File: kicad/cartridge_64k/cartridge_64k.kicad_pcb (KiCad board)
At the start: 2 copper layers, 39 x 102.2 mm, 12 parts, among them J1 Card edge (87715-9106 mate), U1 ATF22V10C-7PX, U2 AT28C256-15PU, U3 AT28C256-15PU, U4 AS7C256C-15PCN, U5 AS7C256C-15PCN

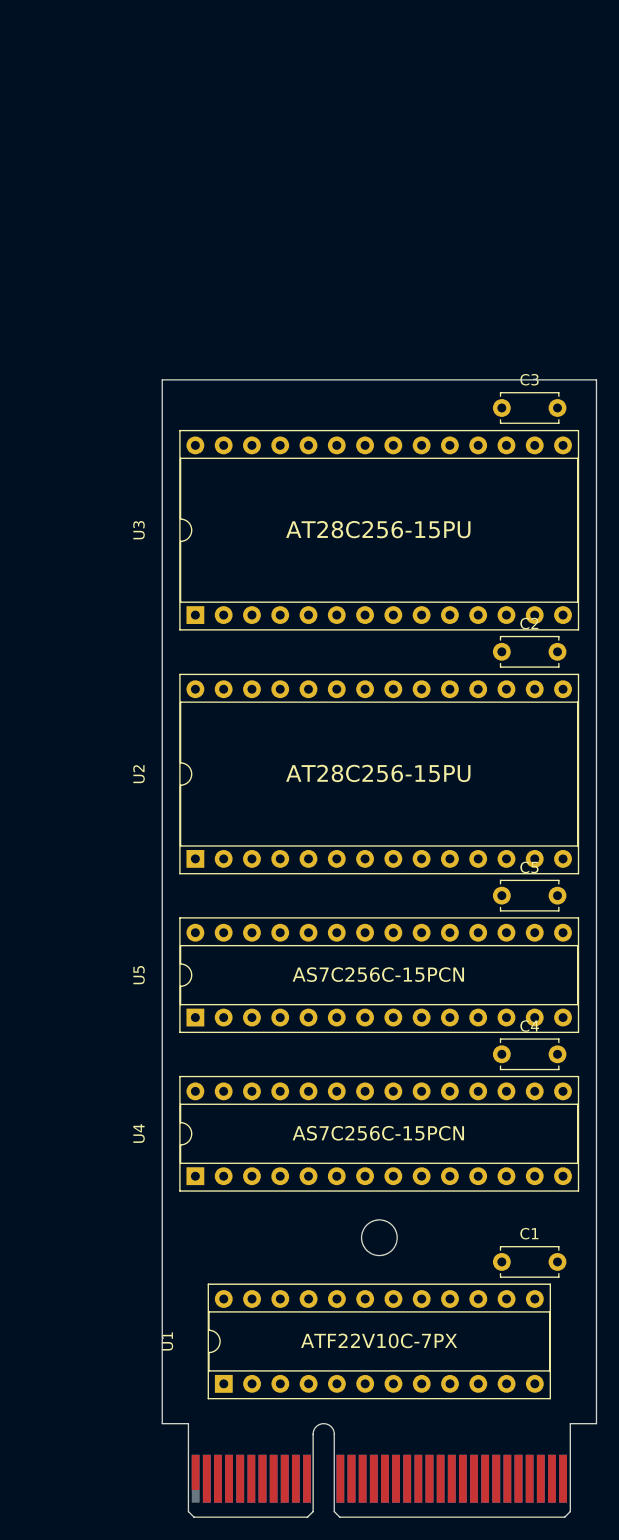
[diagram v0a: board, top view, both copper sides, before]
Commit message: Commit Justin's filled boards: routed carts, J8 reroute, J4 Hirose, library links
The three boards as Justin saved them after zone fill, teardrops and a
clean DRC (2026-10-26): both cartridges 4-layer routed, main board J8
rerouted for the new cartridge pinout, J4 swapped to the Hirose SD socket,
and every footprint linked to the placard library.

Co-Authored-By: Claude Opus 5.5 <noreply@anthropic.com>
Claude-Session: https://claude.ai/code/session_017okF1JiLRNFTfH7Az85hff
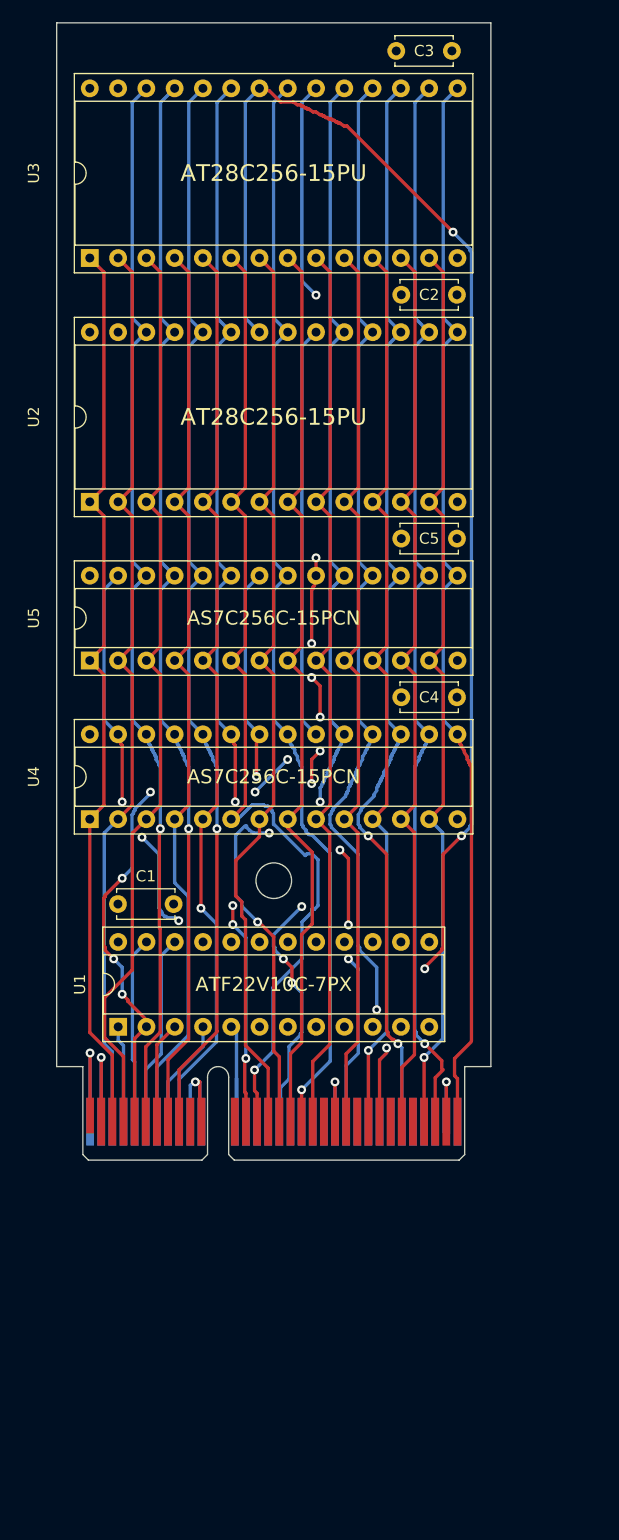
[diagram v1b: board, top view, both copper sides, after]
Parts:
- C1, C2, C3, C4, C5: footprint Capacitor_THT:C_Disc_D5.0mm_W2.5mm_P5.00mm -> placard:C_Disc_D5.0mm_W2.5mm_P5.00mm
- H1: footprint MountingHole:MountingHole_3.2mm_M3 -> placard:MountingHole_3.2mm_M3
- moved C1 47.1 mm to (96.0, 144.9)
- moved J1 33.4 mm to (93.5, 164.5)
- moved C3 33.4 mm to (121.0, 68.3)
- moved H1 33.4 mm to (110.0, 142.8)
- moved U1 33.4 mm to (96.0, 156.0)
- moved U2 33.4 mm to (93.5, 108.8)
- moved U3 33.4 mm to (93.5, 86.9)
- moved U4 33.4 mm to (93.5, 137.3)
- moved U5 33.4 mm to (93.5, 123.1)
- moved C4 33.3 mm to (121.5, 126.4)
- moved C5 33.3 mm to (121.5, 112.1)
- moved C2 33.3 mm to (121.5, 90.2)
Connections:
- J1 pad A10: /A14 -> (no net)
- J1 pad A12: /D0 -> (no net)
- J1 pad A13: /D2 -> /A11
- J1 pad A14: /D4 -> /A4
- J1 pad A15: /D6 -> /A3
- J1 pad A16: /~{CE_LO} -> /~{ROM_OE}
- J1 pad A17: /~{ROM_OE} -> /A2
- J1 pad A18: Net-(J1-PIXEL_ENABLE) -> /A10
- J1 pad A19: Net-(J1-RUN) -> /A1
- J1 pad A20: Net-(J1-CLK) -> (no net)
- J1 pad A22: unconnected-(J1-spare-PadA22) -> /A0
- J1 pad A24: unconnected-(J1-spare-PadA24) -> /D0
- J1 pad A25: unconnected-(J1-spare-PadA25) -> /D6
- J1 pad A27: unconnected-(J1-spare-PadA27) -> /D1
- J1 pad A29: unconnected-(J1-spare-PadA29) -> /D2
- J1 pad A3: /A0 -> /A14
- J1 pad A30: unconnected-(J1-spare-PadA30) -> /D4
- J1 pad A32: unconnected-(J1-spare-PadA32) -> /D3
- J1 pad A4: /A2 -> /A7
- J1 pad A5: /A4 -> /~{CE_LO}
- J1 pad A6: /A6 -> /A13
- J1 pad A7: /A8 -> Net-(J1-PIXEL_ENABLE)
- J1 pad A8: /A10 -> /A8
- J1 pad A9: /A12 -> /A9
- J1 pad B12: /D1 -> Net-(J1-STALL_IN)
- J1 pad B13: /D3 -> (no net)
- J1 pad B14: /D5 -> (no net)
- J1 pad B15: /D7 -> (no net)
- J1 pad B17: Net-(J1-STALL_IN) -> (no net)
- J1 pad B18: Net-(J1-STALL_OUT) -> (no net)
- J1 pad B19: Net-(J1-PC_ENABLE) -> (no net)
- J1 pad B22: unconnected-(J1-spare-PadB22) -> /D7
- J1 pad B27: unconnected-(J1-spare-PadB27) -> /D5
- J1 pad B3: /A1 -> /A12
- J1 pad B4: /A3 -> Net-(J1-CLK)
- J1 pad B5: /A5 -> Net-(J1-STALL_OUT)
- J1 pad B6: /A7 -> Net-(J1-RUN)
- J1 pad B7: /A9 -> /A6
- J1 pad B8: /A11 -> Net-(J1-PC_ENABLE)
- J1 pad B9: /A13 -> /A5
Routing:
- net /~{EE_OE}: track 0.00 -> 130.9 mm, vias 0 -> 3
- net /D6: track 0.00 -> 98.9 mm, vias 0 -> 2
- net /D7: track 0.00 -> 98.5 mm, vias 0 -> 4
- net /D5: track 0.00 -> 98.3 mm, vias 0 -> 2
- net /~{CE_HI}: track 0.00 -> 98.2 mm, vias 0 -> 10
- net /A10: track 0.00 -> 97.8 mm, vias 0 -> 1
- net /A9: track 0.00 -> 97.0 mm, vias 0 -> 1
- net /D4: track 0.00 -> 96.8 mm, vias 0 -> 1
- net /A13: track 0.00 -> 96.5 mm, vias 0 -> 1
- net /A8: track 0.00 -> 96.3 mm, vias 0 -> 1
- net /A11: track 0.00 -> 96.3 mm, vias 0 -> 4
- net /D3: track 0.00 -> 96.2 mm
- net /A4: track 0.00 -> 90.0 mm, vias 0 -> 1
- net /~{CE_LO}: track 0.00 -> 85.9 mm, vias 0 -> 6
- net /A7: track 0.00 -> 83.0 mm
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- added copper zone on In2.Cu, net +5V
- added copper zone on In1.Cu, net GND
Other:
- copper layers 2 -> 4

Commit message: Boards rev A with part numbers PLC-1001/1002/1003 and an S/N box
Silk block on each board (main front by the logo, carts on side B under the
title): PLC-100x REV A, an S/N label and a 17 x 5.5 mm box for a sticker or
paint pen. Board title blocks rev A with the part numbers; schematic title
blocks rev A with PCB/assembly numbers (gen_kicad_schematic.py); BOM bare-PCB
lines carry PLC-100x rev A and assemblies PLC-200x (gen_bom.py).

Co-Authored-By: Claude Opus 5.5 <noreply@anthropic.com>
Claude-Session: https://claude.ai/code/session_01DnW5SVDcRaZyJAhMGzz1W1
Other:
- board text added: "PLC-1003 REV A"
- board text added: "S/N"
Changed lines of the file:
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@@
 	(title_block
 		(title "PLACARD ROM cartridge, 64K")
-		(date "2026-10-26")
-		(rev "1")
+		(date "2026-10-29")
+		(rev "A")
 		(comment 1 "Placed by src/scripts/gen_kicad_cart_pcb.py; not routed")
+		(comment 2 "PCB PLC-1003, assembly PLC-2003")
 	)
 	(layers
@@
 		(layer "Edge.Cuts")
 	)
+	(gr_text "PLC-1003 REV A"
+		(at 110.015 74.9 0)
+		(layer "B.SilkS")
+		(effects
+			(font
+				(size 1.5 1.5)
+				(thickness 0.225)
+			)
+			(justify mirror)
+		)
+	)
+	(gr_text "S/N"
+		(at 116.815 79.55 0)
+		(layer "B.SilkS")
+		(effects
+			(font
+				(size 1.5 1.5)
+				(thickness 0.225)
+			)
+			(justify right mirror)
+		)
+	)
+	(gr_rect
+		(start 99.015 76.8)
+		(end 116.015 82.3)
+		(stroke
+			(width 0.15)
+			(type solid)
+		)
+		(fill no)
+		(layer "B.SilkS")
+	)
 	(gr_text "side B"

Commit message: Carts: Justin's schematic update and refill, H1 restored; fab files regenerated
Update PCB from Schematic renamed the nets (ADDR*/DATABUS*), named the spare
fingers and added part fields, and removed the mounting hole H1 (not in the
cart schematics). H1 is put back at its old position (same uuid), zones
refilled. DRC 0/0/0. Copper otherwise unchanged; the 64K cart's stale plane
gap under U4 is now filled.

Co-Authored-By: Claude Opus 5.5 <noreply@anthropic.com>
Claude-Session: https://claude.ai/code/session_01DnW5SVfTC1ykqH1VEPPtnQ
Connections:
- net /A0 renamed /ADDR0
- net /A1 renamed /ADDR1
- net /A10 renamed /ADDR10
- net /A11 renamed /ADDR11
- net /A12 renamed /ADDR12
- net /A13 renamed /ADDR13
- net /A14 renamed /ADDR14
- net /A2 renamed /ADDR2
- net /A3 renamed /ADDR3
- net /A4 renamed /ADDR4
- net /A5 renamed /ADDR5
- net /A6 renamed /ADDR6
- net /A7 renamed /ADDR7
- net /A8 renamed /ADDR8
- net /A9 renamed /ADDR9
- net /D0 renamed /DATABUS0
- net /D1 renamed /DATABUS1
- net /D2 renamed /DATABUS2
- net /D3 renamed /DATABUS3
- net /D4 renamed /DATABUS4
- net /D5 renamed /DATABUS5
- net /D6 renamed /DATABUS6
- net /D7 renamed /DATABUS7
- J1 pad A10: (no net) -> unconnected-(J1-spare-PadA10)
- J1 pad A12: (no net) -> unconnected-(J1-spare-PadA12)
- J1 pad A20: (no net) -> unconnected-(J1-spare-PadA20)
- J1 pad B13: (no net) -> unconnected-(J1-spare-PadB13)
- J1 pad B14: (no net) -> unconnected-(J1-spare-PadB14)
- J1 pad B15: (no net) -> unconnected-(J1-spare-PadB15)
- J1 pad B17: (no net) -> unconnected-(J1-spare-PadB17)
- J1 pad B18: (no net) -> unconnected-(J1-spare-PadB18)
- J1 pad B19: (no net) -> unconnected-(J1-spare-PadB19)
